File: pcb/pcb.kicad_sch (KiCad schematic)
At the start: 40 parts, among them J1 Screw Connector, J10 Conn_02x10_Counter_Clockwise, J11 Conn_01x10, J2 Screw Connector, J3 Screw Connector, J4 Screw Connector, J5 Conn_01x03, J6 Conn_01x03, J7 Conn_01x03, J8 Conn_01x03, J9 Conn_01x03, Q1 IRF9Z34NPBF, Q2 IRF9Z34NPBF, Q3 IRF9Z34NPBF, Q4 IRF9Z34NPBF, Q5 IRF9Z34NPBF, U1 ACS711ELCTR-12AB-T, U2 ACS711ELCTR-12AB-T, U3 ACS711ELCTR-12AB-T, U4 ACS711ELCTR-12AB-T, U5 ACS711ELCTR-12AB-T, U6 TXS0102DCUR, U7 TXS0102DCUR, U8 TXS0102DCUR, U9 NCP718BSNADJT1G

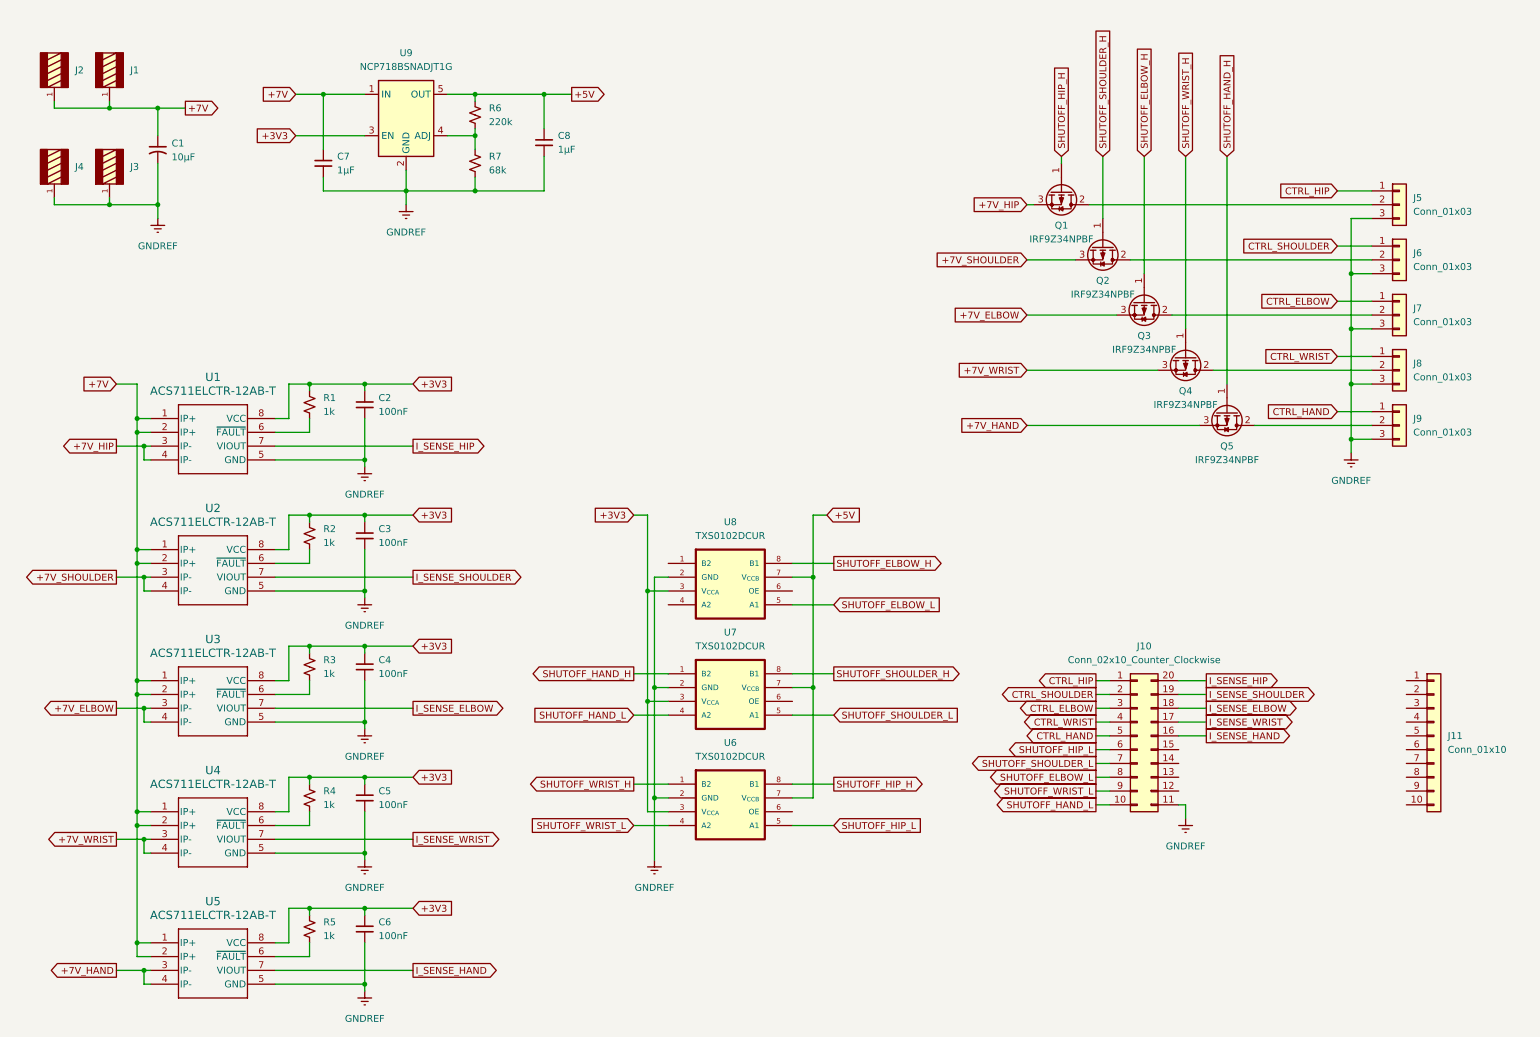
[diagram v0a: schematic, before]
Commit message: Move power supply circuit to hierarchial sheet
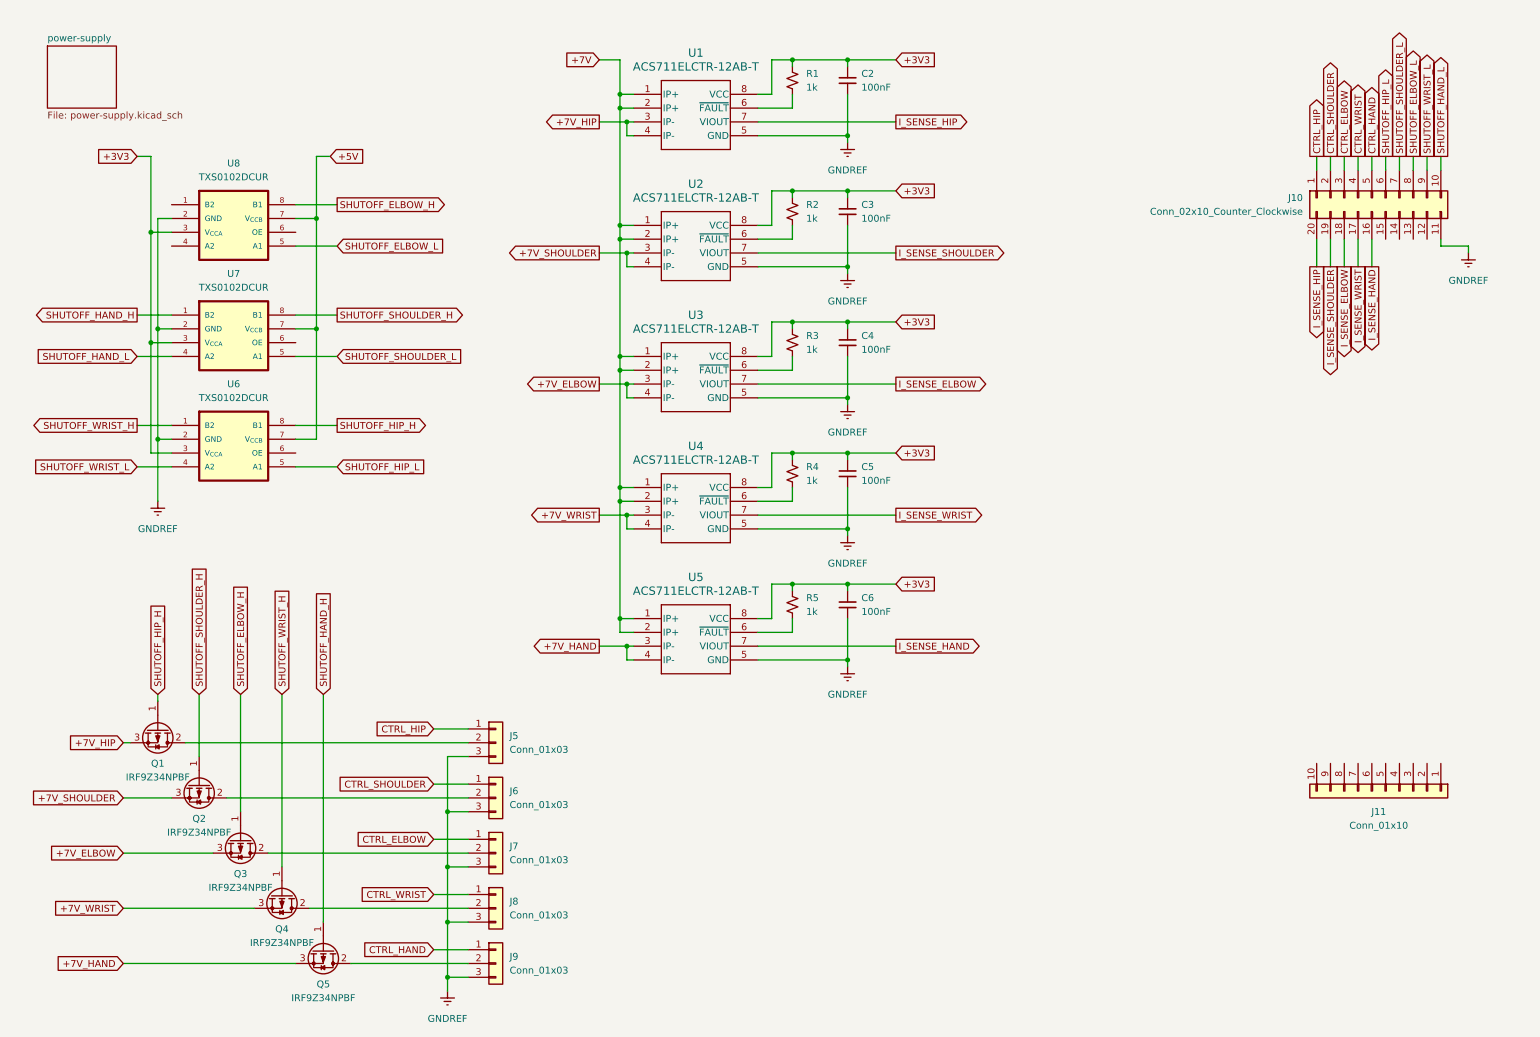
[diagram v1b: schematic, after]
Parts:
- removed C1: 10µF, symbol Device:C_Small_US
- removed C7, C8: 1µF, symbol Device:C_Small
- removed J1, J2, J3, J4: Screw Connector, WP-THRBU_THROUGH-HOLE:WP-THRBU_74650074, symbol WP-THRBU_THROUGH-HOLE:WP-THRBU_THROUGH-HOLE
- removed R6: 220k, symbol Device:R_Small_US
- removed R7: 68k, symbol Device:R_Small_US
- removed U9: NCP718BSNADJT1G, symbol lib:NCP718BSNADJT1G
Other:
- added sheet power-supply (power-supply.kicad_sch)
- moved on the sheet: C2, C3, C4, C5, C6, J10, J11, J5, J6, J7, J8, J9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

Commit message: Add passives for level shifters and enable jumper
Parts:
- added C10, C11: 100nF, symbol Device:C_Small
- added C9: 1µF, symbol Device:C_Small
- added JP1: Jumper_2_Small_Open, symbol Jumper:Jumper_2_Small_Open
- added R10, R8, R9: 10k, symbol Device:R_Small_US
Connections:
- net +3V3: now also C10.1
- net +5V: now also C11.1, C9.1
- net GNDREF: now also C10.2, C11.2, C9.2, R10.2, R8.2, R9.2
- net LVL_SHIFTER_EN: now reaches U7.6 (OE)
- net LVL_SHIFTER_EN: now also U6.6 (OE), U8.6 (OE), JP1.2 (B), R10.1, R8.1, R9.1
- net at J10.12 (Pin_12): now also JP1.1 (A)
- no-connect marks 0 -> 2
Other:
- moved on the sheet: C2, C3, C4, C5, C6, R1, R2, R3, R4, R5, U1, U2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

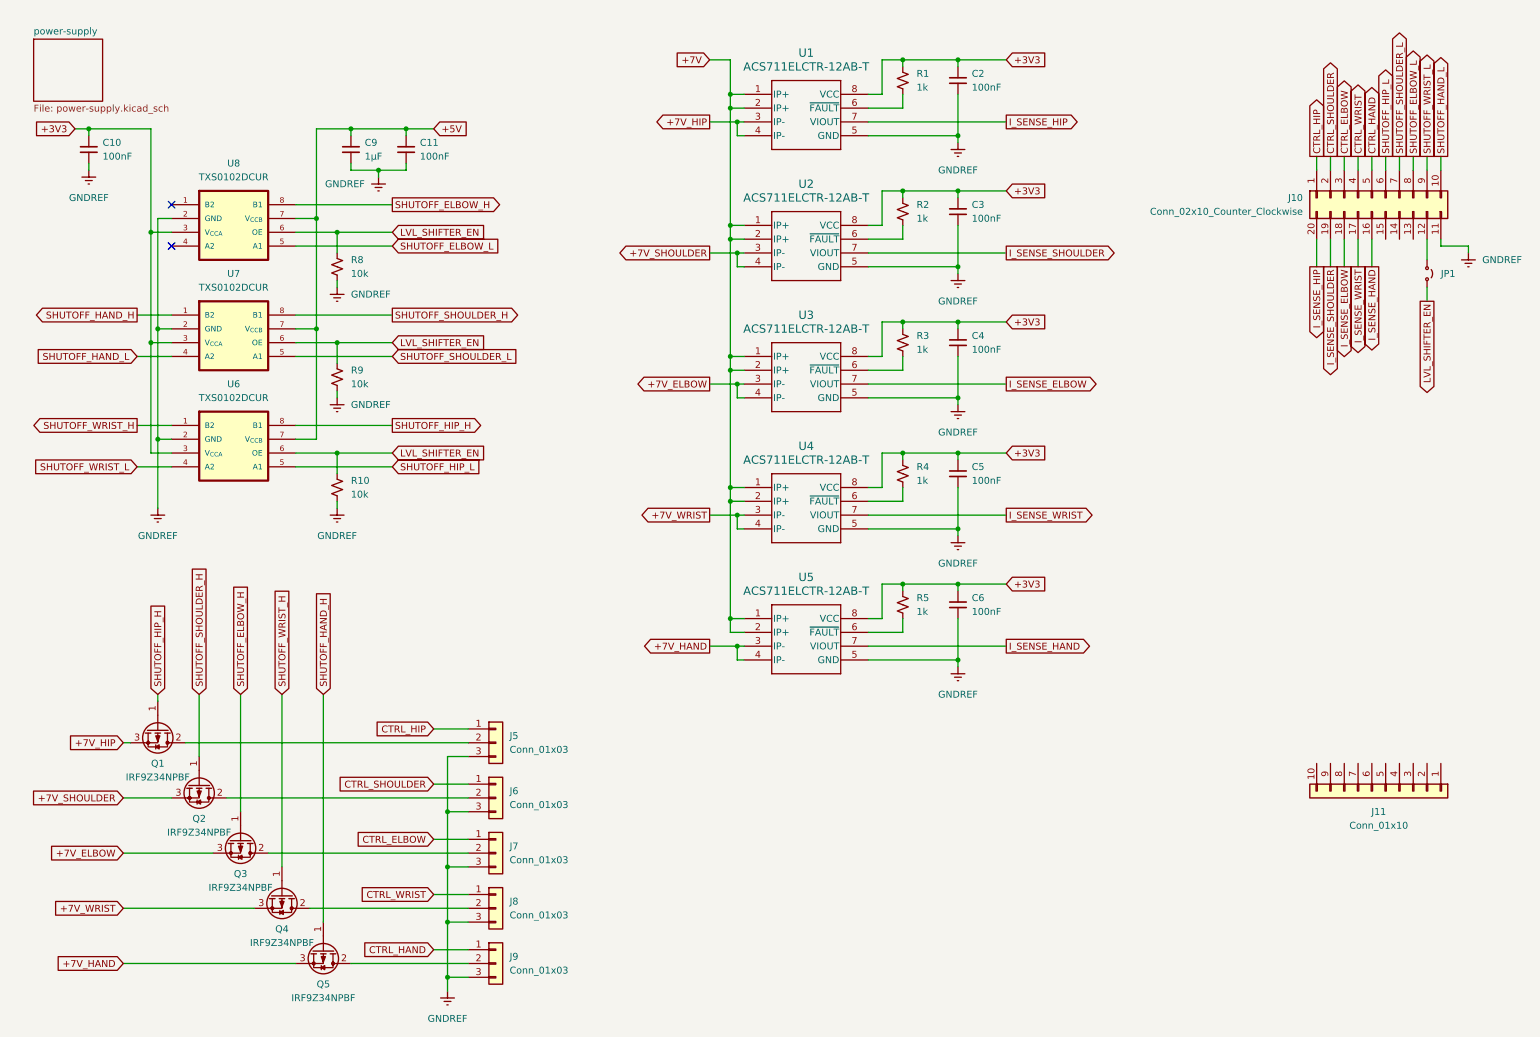
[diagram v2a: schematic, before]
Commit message: Rotate PMOSFET array for readability
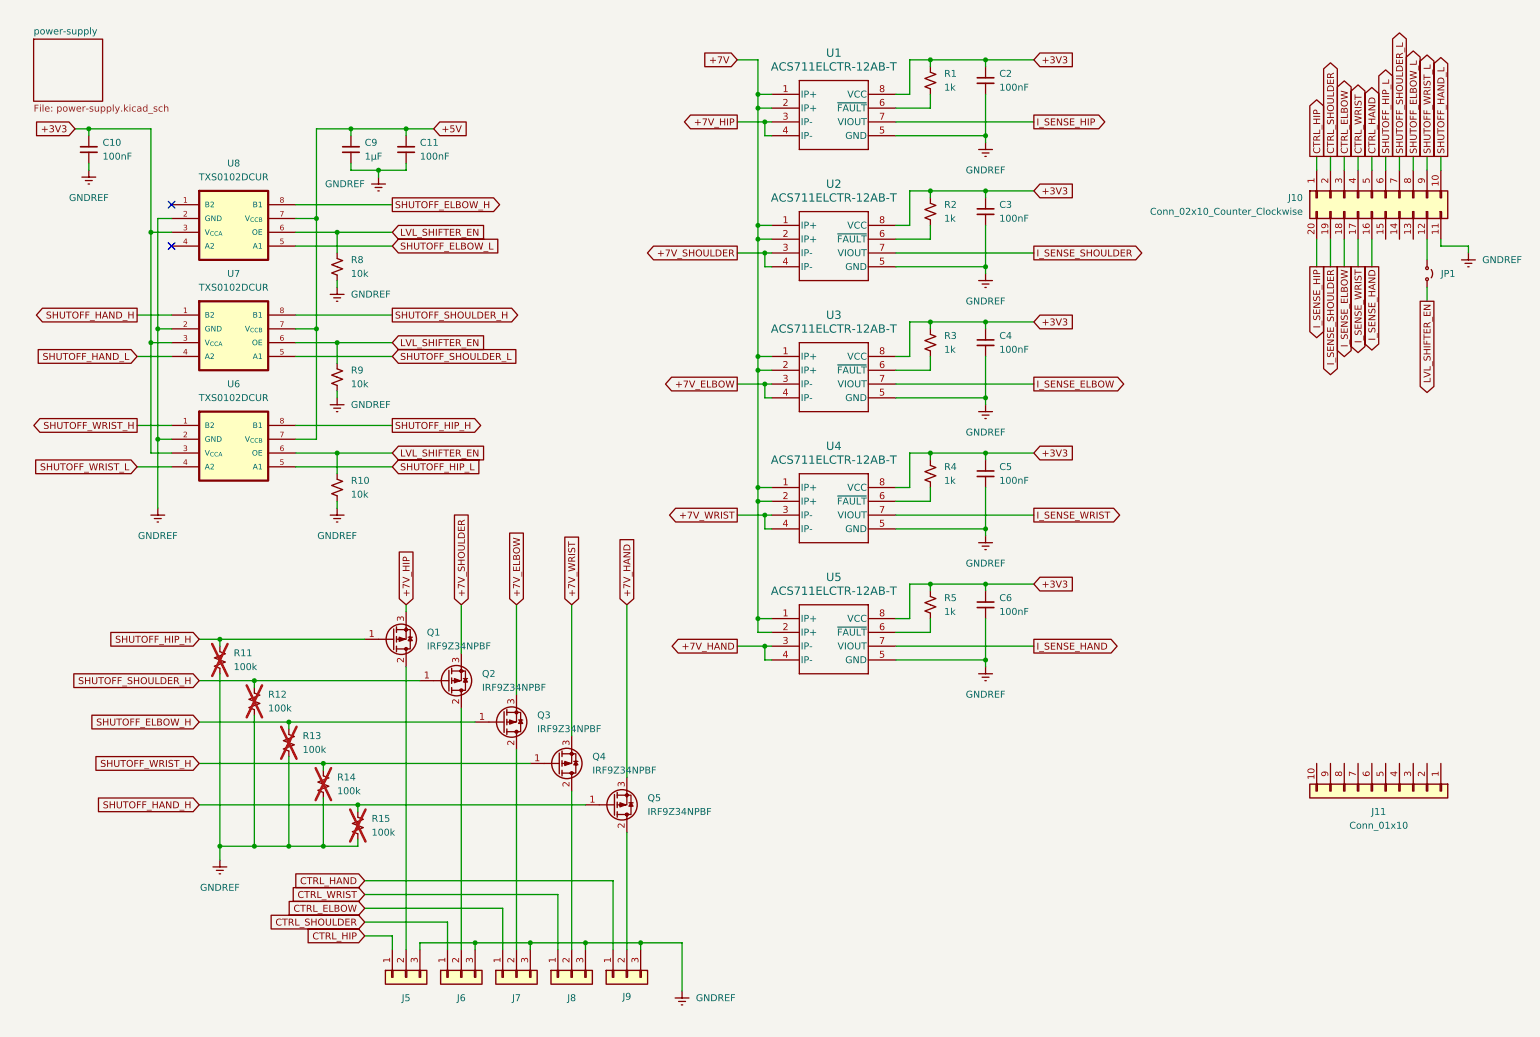
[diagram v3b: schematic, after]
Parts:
- added R11, R12, R13, R14, R15: 100k, symbol Device:R_Small_US
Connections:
- net GNDREF: now also R11.2, R12.2, R13.2, R14.2, R15.2
- net SHUTOFF_ELBOW_H: now also R13.1
- net SHUTOFF_HAND_H: now also R15.1
- net SHUTOFF_HIP_H: now also R11.1
- net SHUTOFF_SHOULDER_H: now also R12.1
- net SHUTOFF_WRIST_H: now also R14.1
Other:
- moved on the sheet: C2, C3, C4, C5, C6, J5, J6, J7, J8, J9, Q1, Q2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

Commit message: Add header labels for UART and 3.3V
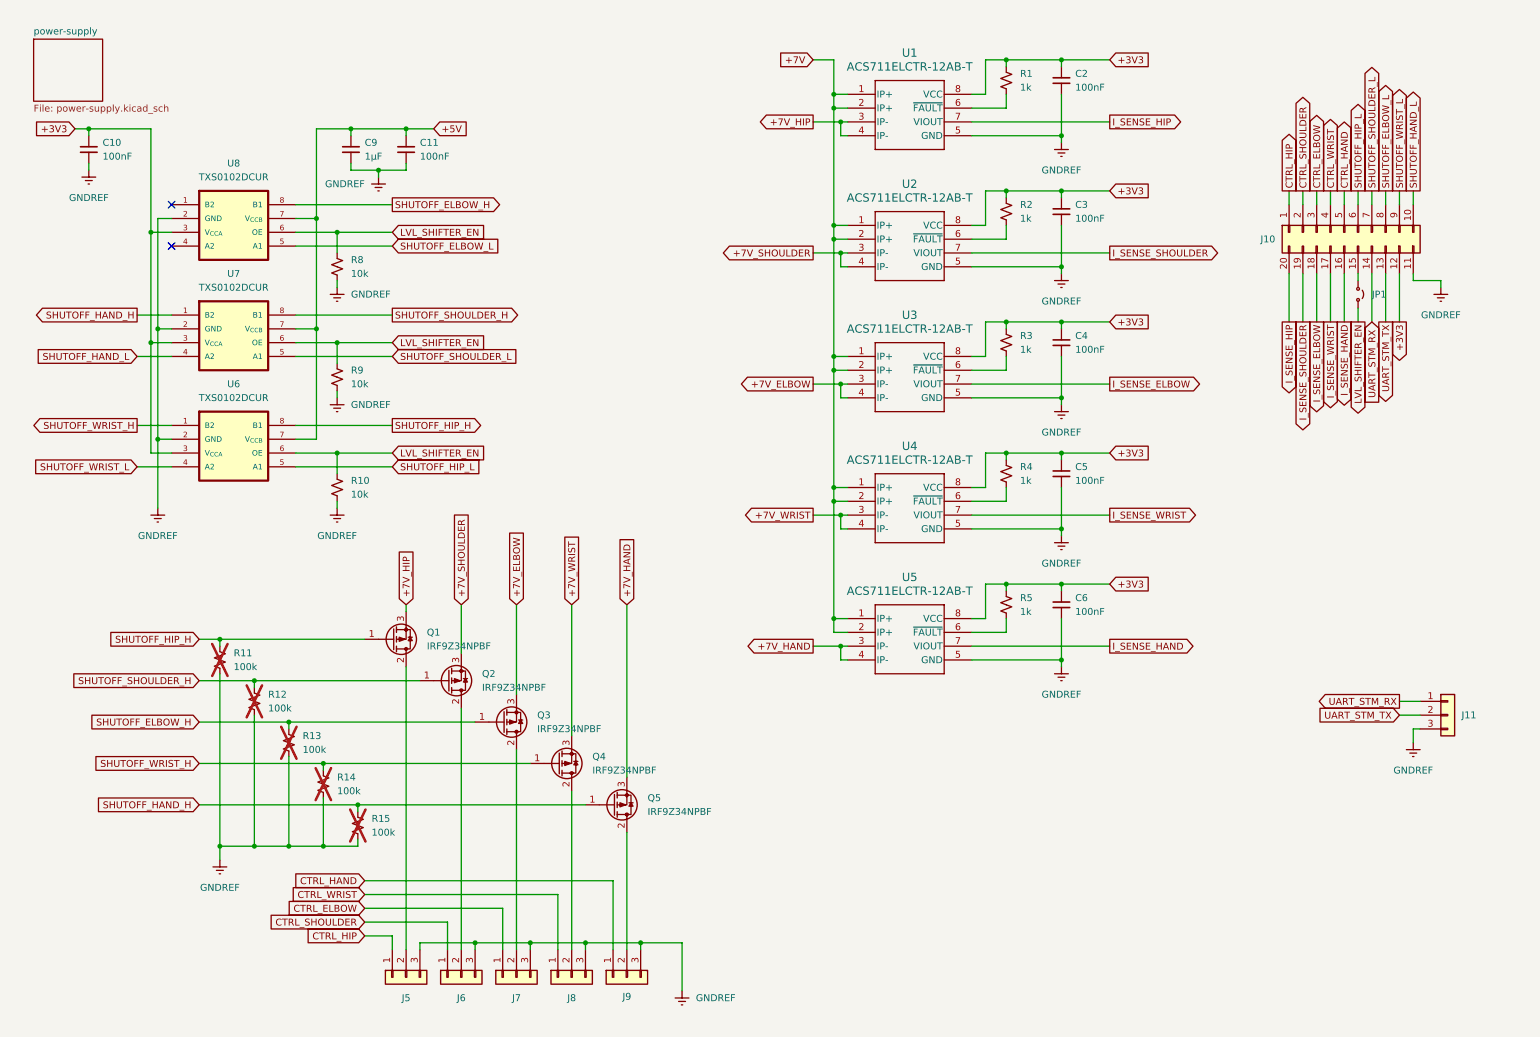
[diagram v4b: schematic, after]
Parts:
- removed J11: Conn_01x10, symbol lib:Conn_01x10
- added J11: Conn_01x03, Connector:Tag-Connect_TC2030-IDC-NL_2x03_P1.27mm_Vertical, symbol Connector_Generic:Conn_01x03
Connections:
- net +3V3: now also J10.12 (Pin_12)
- net GNDREF: now also J11.3 (Pin_3)
- net at JP1.1 (A): now also J10.15 (Pin_15); no longer J10.12 (Pin_12)
- net UART_STM_TX: now reaches J10.13 (Pin_13)
- net UART_STM_TX: now also J11.2 (Pin_2)
- net UART_STM_RX: now reaches J10.14 (Pin_14)
- net UART_STM_RX: now also J11.1 (Pin_1)
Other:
- company: (none) -> ECE 4710 - Vision Arm
- moved on the sheet: C2, C3, C4, C5, C6, J10, JP1, R1, R2, R3, R4, R5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
